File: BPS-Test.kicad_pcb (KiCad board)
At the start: 2 copper layers, 91 x 94 mm, 106 parts, among them J1 Conn_01x02, J10 Conn_01x02, J11 Conn_01x02, J12 Conn_01x02, J13 Conn_01x02, J14 Conn_01x02, J15 Conn_01x02, J16 Conn_01x02, J17 Conn_01x02, J18 Conn_01x02, J19 Conn_01x02, J2 Conn_01x02, J20 Conn_01x02, J21 Conn_01x02, J22 Conn_01x02, J23 Conn_01x07, J24 Conn_01x07, J25 Conn_01x01, J26 Conn_01x01, J3 Conn_01x02, J4 Conn_01x02, J5 Conn_01x02, J6 Conn_01x02, J7 Conn_01x02, J8 Conn_01x02, J9 Conn_01x02

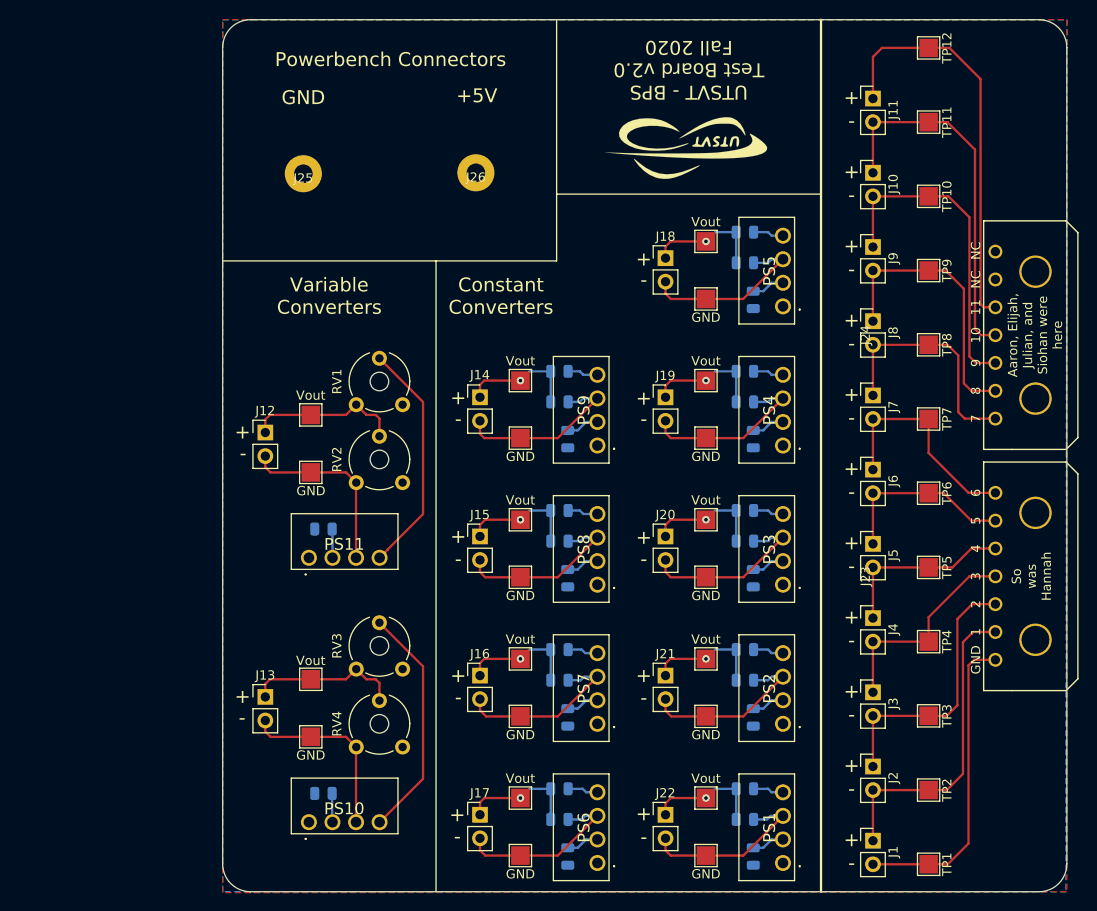
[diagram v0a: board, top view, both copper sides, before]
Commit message: Complete redesign of BPS Test board
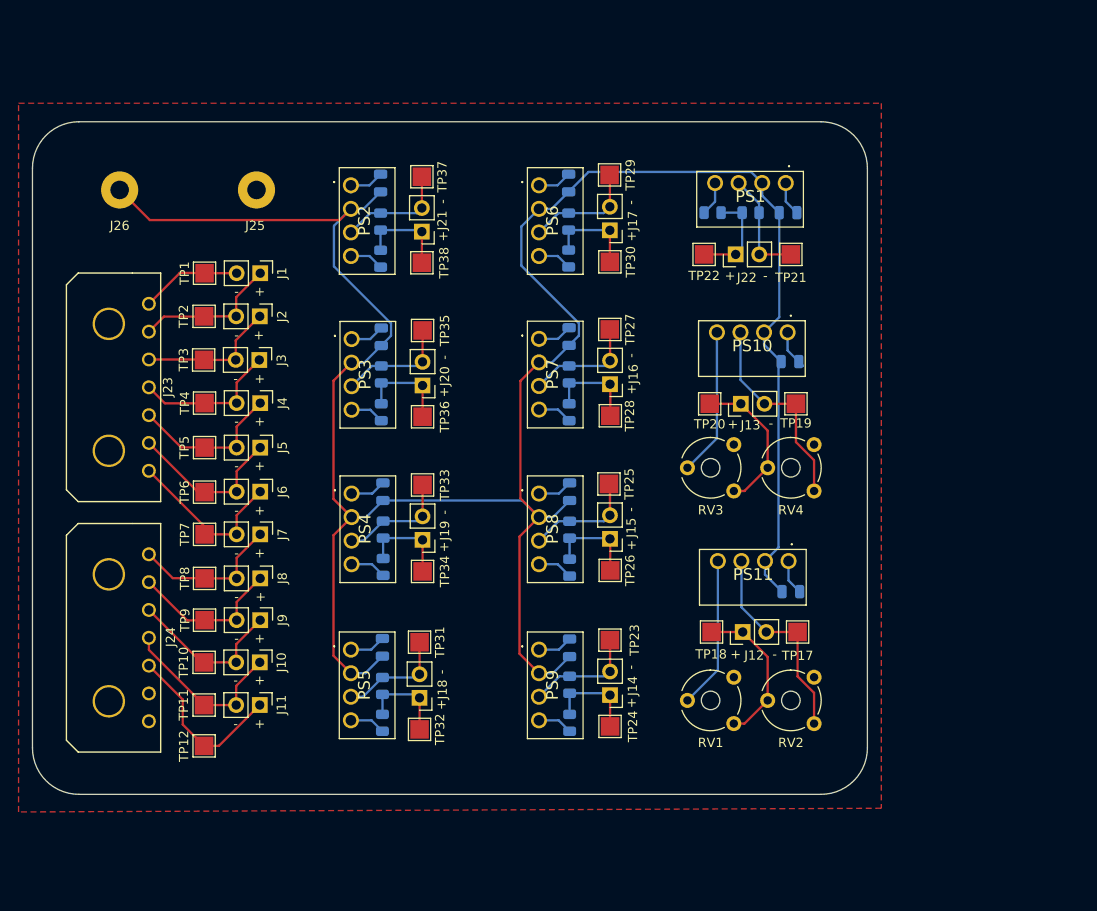
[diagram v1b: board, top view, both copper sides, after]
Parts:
- added G***: LOGO, Lauren:OliveFP, B.Cu at (161.7, 113.7)
- added G***: LOGO, Lauren:NameFP, B.Cu at (164.2, 124.4)
- LOGO2: moved to B.Cu
- R10, R11, R12, R14, R15, R7, R8, R9: value 280 -> 1.4K
- R16, R17, R18, R19, R20, R21, R22, R23, R24: value 720 -> 3.6K
- moved TP12 108.4 mm to (101.0, 122.3), turned to 0 degrees
- moved TP1 100.8 mm to (101.0, 71.3), turned to 0 degrees
- moved TP11 100.2 mm to (101.0, 117.9), turned to 0 degrees
- moved J24 96.9 mm to (95.0, 110.6), turned to 270 degrees
- moved J23 93.5 mm to (95.0, 83.6), turned to 270 degrees
- moved TP2 93.3 mm to (101.0, 76.0), turned to 0 degrees
- moved J11 93.0 mm to (107.0, 117.9), turned to 270 degrees
- moved TP10 92.9 mm to (101.0, 113.3), turned to 0 degrees
- moved J1 90.0 mm to (107.0, 71.3), turned to 270 degrees
- moved LOGO2 88.0 mm to (93.2, 122.0)
- moved TP3 87.1 mm to (101.0, 80.7), turned to 0 degrees
- moved TP9 86.7 mm to (101.0, 108.7), turned to 0 degrees
- moved J10 84.6 mm to (107.0, 113.3), turned to 270 degrees
- moved TP4 82.2 mm to (101.0, 85.3), turned to 0 degrees
- moved TP8 82.0 mm to (101.0, 104.2), turned to 0 degrees
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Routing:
- net +5V: track 38.4 -> 257.1 mm
- net GND: track 0.00 -> 44.2 mm
- net Net-(J11-Pad1): track 43.9 -> 18.9 mm
- net Net-(J1-Pad2): track 33.6 -> 10.8 mm
- net Net-(J10-Pad1): track 39.5 -> 19.0 mm
- net Net-(J1-Pad1): track 34.0 -> 15.8 mm
- net Net-(J10-Pad2): track 35.0 -> 17.4 mm
- net Net-(J2-Pad1): track 29.1 -> 15.2 mm
- net Net-(J24-Pad6): track 30.2 -> 16.7 mm
- net Net-(J24-Pad7): track 25.9 -> 16.3 mm
- net Net-(PS10-Pad4): track 25.4 -> 15.9 mm
- net Net-(PS11-Pad4): track 25.4 -> 16.4 mm
- net Net-(J18-Pad2): track 19.3 -> 11.9 mm
- net Net-(J22-Pad2): track 19.3 -> 12.0 mm
- net Net-(J14-Pad2): track 19.3 -> 12.2 mm
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- added copper zone on F.Cu, net GND
- removed copper zone on F.Cu, net +5V
- removed copper zone on B.Cu, net GND
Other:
- board size 91 x 94 mm -> 90 x 72.5 mm
- board text removed: "+5V"
- board text removed: "1"
- board text removed: "10"
- board text removed: "11"
- board text removed: "2"
- board text removed: "3"
- board text removed: "4"
- board text removed: "5"
- board text removed: "6"
- board text removed: "7"
- board text removed: "8"
- board text removed: "9"
- board text removed: "Aaron, Elijah, Julian, and Siohan were here"
- board text removed: "Constant Converters"
- board text removed: "Dr. Gary Hallock"
- board text removed: "GND"
- board text removed: "NC"
- board text removed: "Powerbench Connectors"
- board text removed: "So was Hannah"
- board text removed: "UTSVT - BPS Test Board v2.0 Fall 2020"
- board text removed: "Variable Converters"
- board text removed: "Vout"
